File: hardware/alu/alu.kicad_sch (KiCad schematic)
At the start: 405 parts, among them J8 Conn_02x24_Odd_Even, Q100 IRLML6402, Q101 IRLML6244, Q102 IRLML6402, Q103 IRLML6244, Q104 IRLML6402, Q105 IRLML6244, Q106 IRLML6402, Q107 IRLML6244, Q108 IRLML6402, Q109 IRLML6244, Q110 IRLML6402, Q111 IRLML6244, Q112 IRLML6402, Q113 IRLML6244, Q114 IRLML6402, Q115 IRLML6244, Q116 IRLML6402, Q117 IRLML6244, Q118 IRLML6402, Q119 IRLML6244, Q120 IRLML6402, Q121 IRLML6244, Q122 IRLML6402, Q123 IRLML6244, Q124 IRLML6402, Q125 IRLML6244, Q126 IRLML6402, Q127 IRLML6244, Q128 IRLML6402, Q129 IRLML6244, Q130 IRLML6402, Q131 IRLML6244, Q132 IRLML6402, Q133 IRLML6244, Q134 IRLML6402, Q135 IRLML6244, Q136 IRLML6402, Q137 IRLML6244, Q138 IRLML6402, Q139 IRLML6244, Q140 IRLML6402, Q141 IRLML6244, Q142 IRLML6402, Q143 IRLML6244, Q144 IRLML6402, Q145 IRLML6244, Q146 IRLML6402, Q147 IRLML6244, Q148 IRLML6402, Q149 IRLML6244, Q150 IRLML6402, Q151 IRLML6244, Q152 IRLML6402, Q153 IRLML6244, Q154 IRLML6402, Q155 IRLML6244, Q156 IRLML6402, Q157 IRLML6244, Q158 IRLML6402, Q159 IRLML6244, Q160 IRLML6402, Q161 IRLML6244, Q162 IRLML6402, Q163 IRLML6244, Q164 IRLML6402, Q165 IRLML6244, Q166 IRLML6402, Q167 IRLML6244, Q168 IRLML6402, Q169 IRLML6244, Q170 IRLML6402, Q171 IRLML6244, Q172 IRLML6402, Q173 IRLML6244, Q174 IRLML6402, Q175 IRLML6244, Q176 IRLML6402, Q93 IRLML6402, Q94 IRLML6244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

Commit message: more WIP work on ALU V2
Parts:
- added C91, C93, C94, C95: 330nF, Capacitor_SMD:C_0402_1005Metric, symbol Device:C
- J8: footprint Connector_PinSocket_2.54mm:PinSocket_2x24_P2.54mm_Horizontal -> Connector_PinHeader_2.54mm:PinHeader_2x24_P2.54mm_Horizontal
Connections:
- net +5V: now also C91.1, C93.1, C94.1, C95.1
- net GND: now also C91.2, C93.2, C94.2, C95.2

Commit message: ALU V2 done?
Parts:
- C1, C10, C11, C12, C13, C14, C15, C16, C17, C18, C19, C2, C20, C21, C22, C23, C24, C25, C26, C27, C28, C29, C3, C30, C31, C32, C33, C34, C35, C4, C40, C41, C42, C43, C44, C45, C46, C47, C5, C50, C51, C52, C53, C54, C55, C56, C57, C58, C59, C6, C60, C61, C62, C63, C64, C65, C66, C67, C68, C69, C7, C70, C71, C72, C73, C77, C78, C79, C8, C80, C81, C82, C83, C84, C85, C9, C90, C91, C92, C93, C94, C95: LCSC C2918485 -> C5448882
- D137, D138, D139, D140, D141, D142, D143, D144, D145, D146, D147, D148, D149, D150, D30, D31, D32, D33, D34, D35, D36, D37, D38, D39, D40, D41, D42, D43, D44, D45, D46, D47, D48, D49, D50, D51, D63, D89, D90, D91, D92, D93: LCSC C84267 -> C965793
- Q100, Q102, Q104, Q106, Q108, Q110, Q112, Q114, Q116, Q118, Q120, Q122, Q124, Q126, Q128, Q130, Q132, Q134, Q136, Q138, Q140, Q142, Q144, Q146, Q148, Q150, Q152, Q154, Q156, Q158, Q160, Q162, Q164, Q166, Q168, Q170, Q172, Q174, Q176, Q93, Q96, Q98: LCSC (none) -> C2886430
- R1, R10, R11, R12, R13, R14, R15, R16, R17, R18, R19, R2, R20, R21, R3, R4, R5, R6, R7, R8, R9: LCSC (none) -> C60490
- R107, R108, R109, R110, R111, R112, R113, R114, R115, R116, R117, R118, R119, R120, R121, R122, R123, R124, R125, R126, R127, R128, R129, R130, R131, R132, R133, R134, R135, R136, R137, R138, R139, R140, R141, R142, R143, R144, R145, R146, R147, R148, R149, R150, R151, R152, R153, R154, R155, R156, R157, R158, R159, R160, R161, R162, R163, R164, R165, R166, R167, R168, R169, R170, R171, R172, R173, R174, R175, R176, R177, R178, R179, R180, R181, R182, R183, R184, R185, R186, R187, R188, R189, R190, R191: LCSC C21190 -> C106235
- U42, U43, U50, U51, U52, U53, U54, U55, U58, U59, U60, U61, U62, U63, U66, U67, U71, U84, U85, U86, U88, U89, U90, U91: LCSC (none) -> C6823
- U68: LCSC (none) -> C5620
- U72, U73, U74, U75, U83, U87: LCSC (none) -> C5586

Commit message: small fixes in ALU V2, started work on register fabric, schematic done (?)
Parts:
- added D52: LED, LED_SMD:LED_0402_1005Metric, symbol Device:LED
- added R192: 1000, Resistor_SMD:R_0402_1005Metric, symbol Device:R
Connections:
- net +5V: now also D52.2 (A)
- net GND: now also R192.1
- new net: D52.1 (K), R192.2

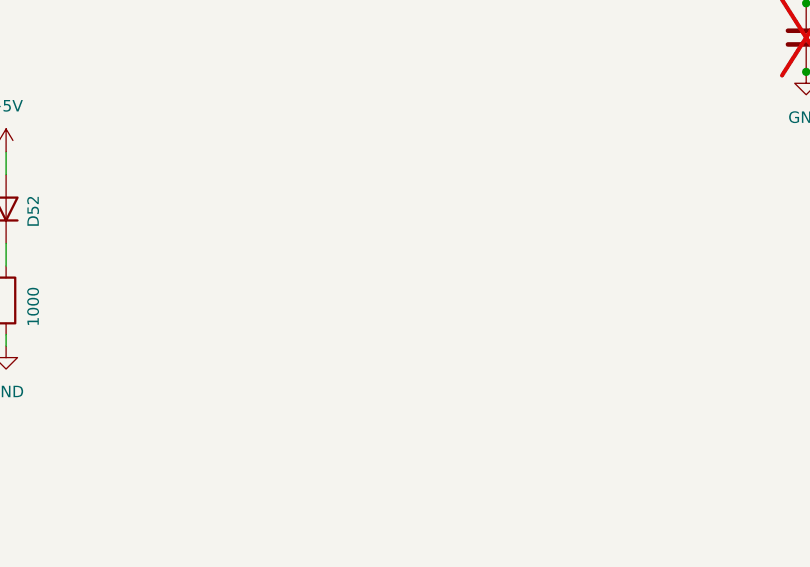
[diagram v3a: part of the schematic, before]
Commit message: fixed ALU order of Op bits, finished register fabric schematic
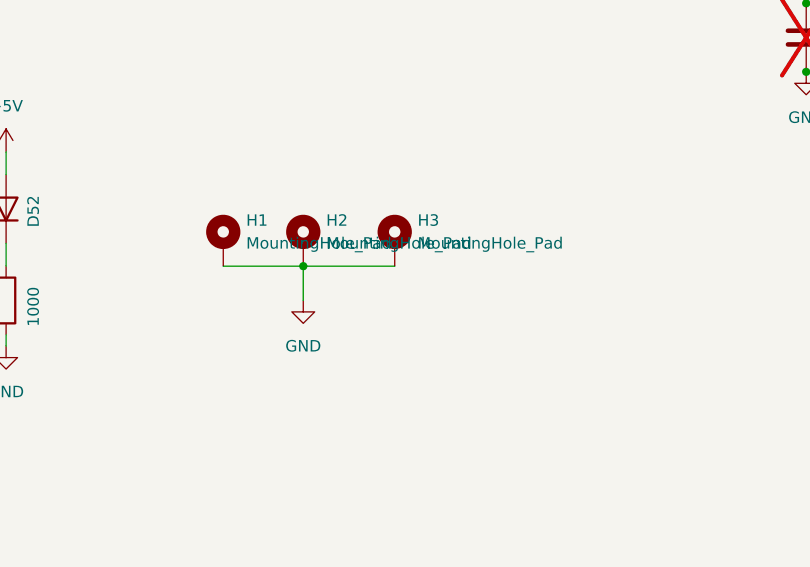
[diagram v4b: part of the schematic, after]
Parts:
- added H1, H2, H3: MountingHole_Pad, MountingHole:MountingHole_3.2mm_M3_ISO7380_Pad_TopBottom, symbol Mechanical:MountingHole_Pad
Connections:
- net GND: now also H1.1, H2.1, H3.1

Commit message: small fixes on register fabric
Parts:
- R1, R10, R11, R12, R13, R14, R15, R16, R17, R18, R19, R2, R20, R21, R3, R4, R5, R6, R7, R8, R9: value 10K -> 100K
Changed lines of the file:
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@@
 			)
 		)
-		(property "Value" "10K"
+		(property "Value" "100K"
 			(at 275.59 1275.0799 0)
 			(effects
@@
 			)
 		)
-		(property "Value" "10K"
+		(property "Value" "100K"
 			(at 391.16 1164.5899 0)
 			(effects
@@
 			)
 		)
-		(property "Value" "10K"
+		(property "Value" "100K"
 			(at 275.59 1164.5899 0)
 			(effects
@@
 			)
 		)
-		(property "Value" "10K"
+		(property "Value" "100K"
 			(at 275.59 1060.4499 0)
 			(effects
@@
 			)
 		)
-		(property "Value" "10K"
+		(property "Value" "100K"
 			(at 467.36 1164.5899 0)
 			(effects
@@
 			)
 		)
-		(property "Value" "10K"
+		(property "Value" "100K"
 			(at 237.49 1060.4499 0)
 			(effects
@@
 			)
 		)
-		(property "Value" "10K"
+		(property "Value" "100K"
 			(at 353.06 1164.5899 0)
 			(effects
@@
 			)
 		)
-		(property "Value" "10K"
+		(property "Value" "100K"
 			(at 237.49 1164.5899 0)
 			(effects
@@
 			)
 		)
-		(property "Value" "10K"
+		(property "Value" "100K"
 			(at 429.26 1164.5899 0)
 			(effects
@@
 			)
 		)
-		(property "Value" "10K"
+		(property "Value" "100K"
 			(at 353.06 1061.7199 0)
 			(effects
@@
 			)
 		)
-		(property "Value" "10K"
+		(property "Value" "100K"
 			(at 313.69 1164.5899 0)
 			(effects
@@
 			)
 		)
-		(property "Value" "10K"
+		(property "Value" "100K"
 			(at 313.69 1275.0799 0)
 			(effects
@@
 			)
 		)
-		(property "Value" "10K"
+		(property "Value" "100K"
 			(at 237.49 1275.0799 0)
 			(effects
@@
 			)
 		)
-		(property "Value" "10K"
+		(property "Value" "100K"
 			(at 199.39 1164.5899 0)
 			(effects
@@
 			)
 		)
-		(property "Value" "10K"
+		(property "Value" "100K"
 			(at 199.39 1275.0799 0)
 			(effects
@@
 			)
 		)
-		(property "Value" "10K"
+		(property "Value" "100K"
 			(at 391.16 1061.7199 0)
 			(effects
@@
 			)
 		)
-		(property "Value" "10K"
+		(property "Value" "100K"
 			(at 199.39 1060.4499 0)
 			(effects
@@
 			)
 		)
-		(property "Value" "10K"
+		(property "Value" "100K"
 			(at 429.26 1275.0799 0)
 			(effects
@@
 			)
 		)
-		(property "Value" "10K"
+		(property "Value" "100K"
 			(at 391.16 1275.0799 0)
 			(effects
@@
 			)
 		)
-		(property "Value" "10K"
+		(property "Value" "100K"
 			(at 467.36 1275.0799 0)
 			(effects
@@
 			)
 		)
-		(property "Value" "10K"
+		(property "Value" "100K"
 			(at 353.06 1275.0799 0)
 			(effects

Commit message: as ordered
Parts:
- C1, C10, C11, C12, C13, C14, C15, C16, C17, C18, C19, C2, C20, C21, C22, C23, C24, C25, C26, C27, C28, C29, C3, C30, C31, C32, C33, C34, C35, C4, C40, C41, C42, C43, C44, C45, C46, C47, C5, C50, C51, C52, C53, C54, C55, C56, C57, C58, C59, C6, C60, C61, C62, C63, C64, C65, C66, C67, C68, C69, C7, C70, C71, C72, C73, C77, C78, C79, C8, C80, C81, C82, C83, C84, C85, C9, C90, C91, C92, C93, C94, C95: LCSC C5448882 -> C77020
- R1, R10, R11, R12, R13, R14, R15, R16, R17, R18, R19, R2, R20, R21, R3, R4, R5, R6, R7, R8, R9: LCSC C60490 -> C60491
